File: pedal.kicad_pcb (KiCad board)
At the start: 4 copper layers, 39 parts, among them J2 USB_C_Receptacle_USB2.0_16P, SW1 MK-11C04-G013, U1 STM32H745XIH6, U2 TPS631000DRLR, U3 TLV77018PDBVR, U4 TPS2116DRL, U5 USBLC6-2SC6, U6 USBLC6-2SC6, U7 BQ25302, U8 BQ27427YZFR

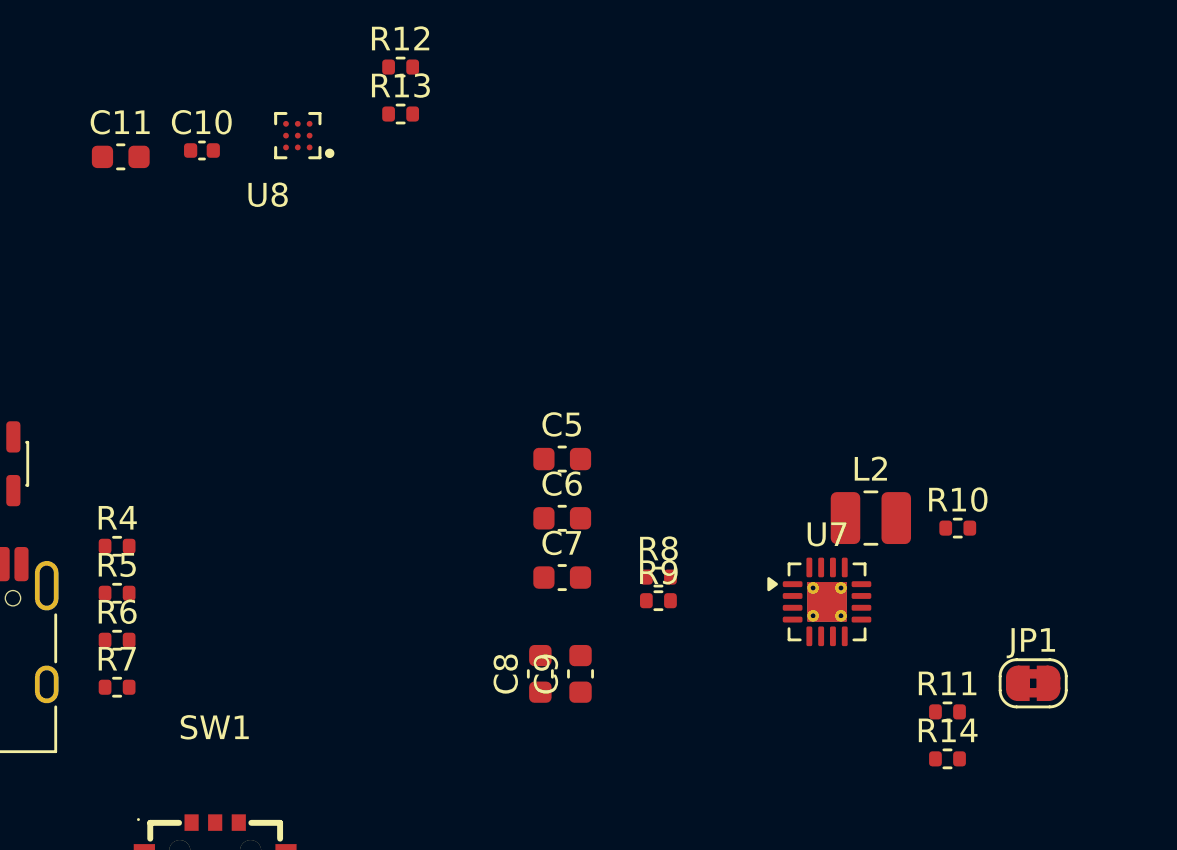
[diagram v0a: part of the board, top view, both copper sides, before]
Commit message: add battery connector model and charge led
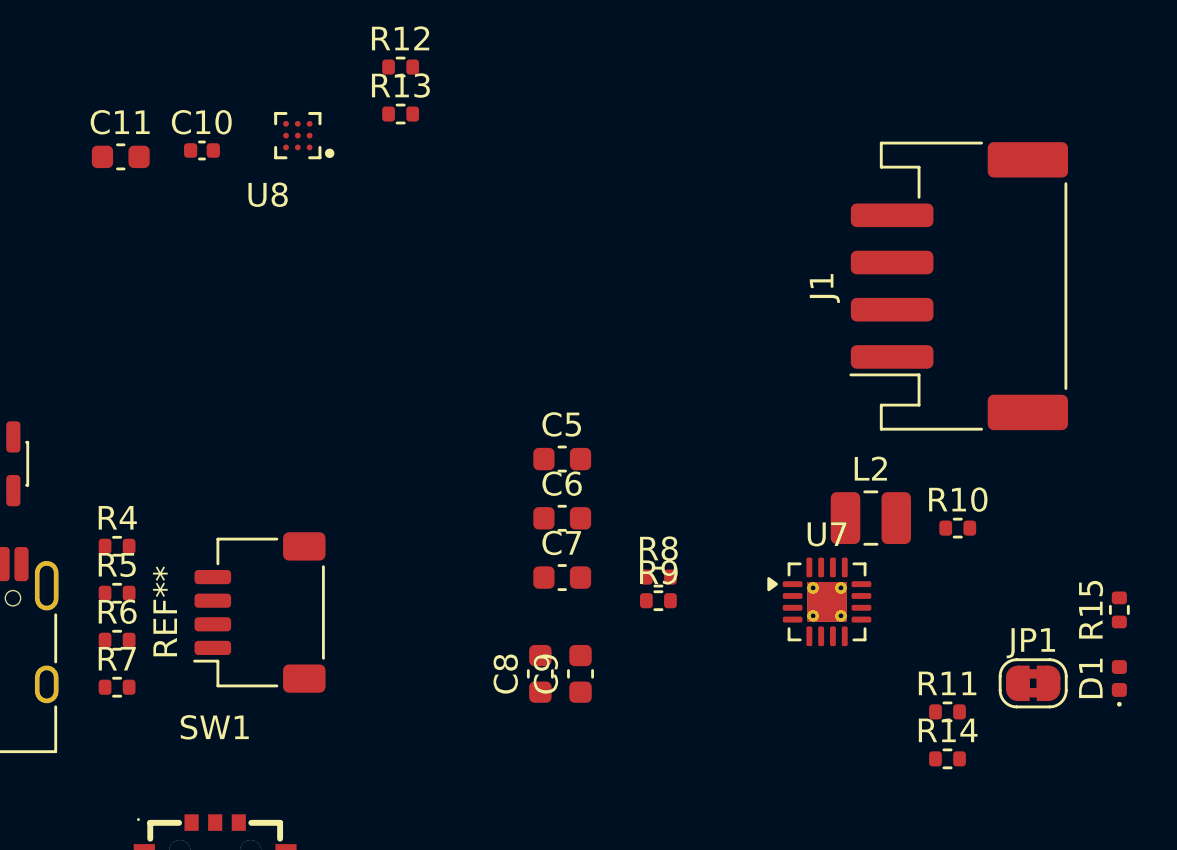
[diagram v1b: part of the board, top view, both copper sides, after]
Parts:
- added D1: CHARGE, LED_SMD:LED_0402_1005Metric, F.Cu at (192.4, 132.9)
- added J1: Battery, Connector_JST:JST_PH_S4B-PH-SM4-TB_1x04-1MP_P2.00mm_Horizontal, F.Cu at (185.6, 116.3)
- added R15: 2.4k, Resistor_SMD:R_0402_1005Metric, F.Cu at (192.4, 130.0)
- added REF**: JST_SH_SM04B-SRSS-TB_1x04-1MP_P1.00mm_Horizontal, Connector_JST:JST_SH_SM04B-SRSS-TB_1x04-1MP_P1.00mm_Horizontal, F.Cu at (156.0, 130.1)

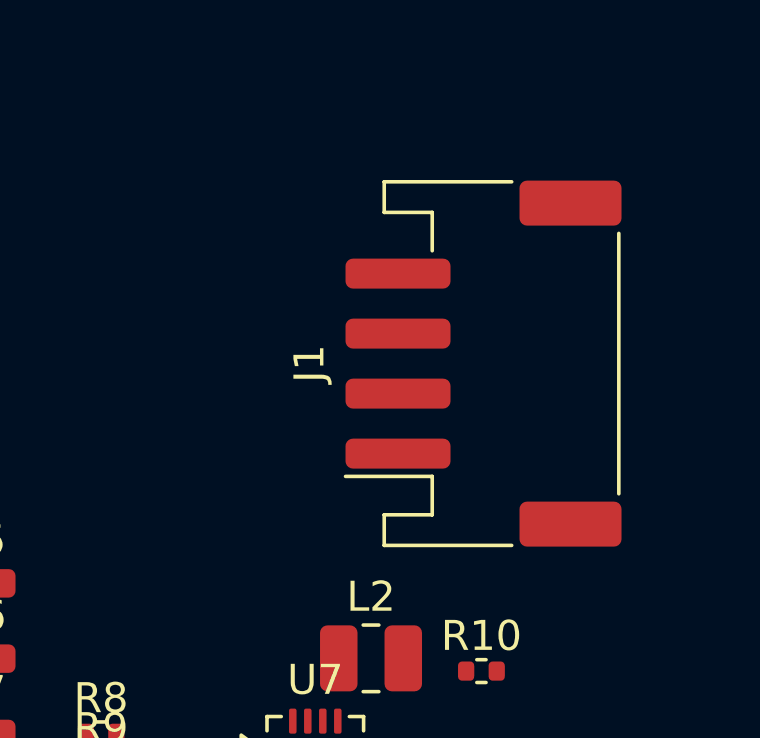
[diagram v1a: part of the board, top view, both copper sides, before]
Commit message: replace battery connector with solder pads
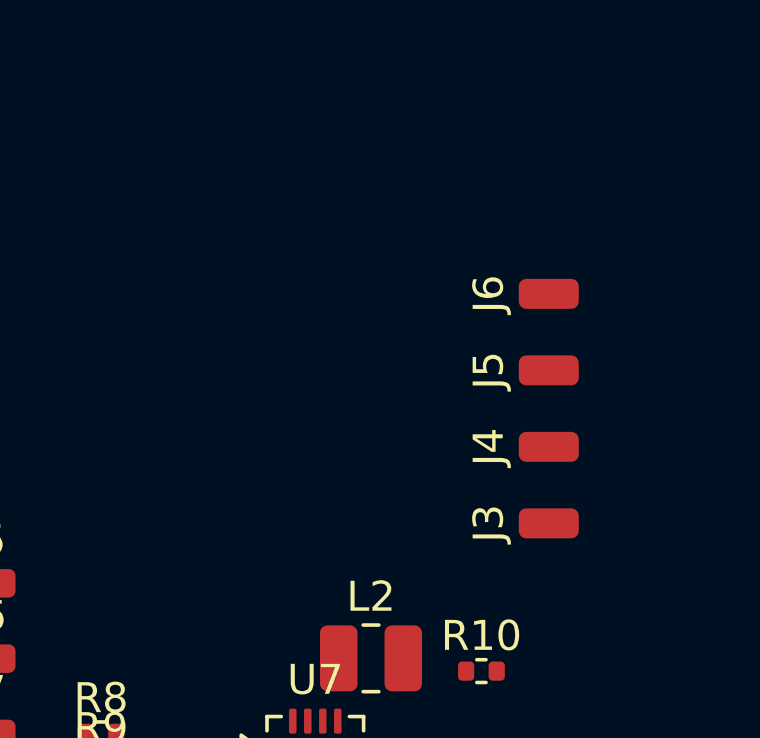
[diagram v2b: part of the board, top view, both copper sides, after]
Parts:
- removed J1: Battery, Connector_JST:JST_PH_S4B-PH-SM4-TB_1x04-1MP_P2.00mm_Horizontal
- added J3: VBATT, Connector_Wire:SolderWirePad_1x01_SMD_1x2mm, F.Cu at (187.8, 121.6)
- added J4: THERM, Connector_Wire:SolderWirePad_1x01_SMD_1x2mm, F.Cu at (187.8, 119.0)
- added J5: GND, Connector_Wire:SolderWirePad_1x01_SMD_1x2mm, F.Cu at (187.8, 116.5)
- added J6: GND, Connector_Wire:SolderWirePad_1x01_SMD_1x2mm, F.Cu at (187.8, 114.0)

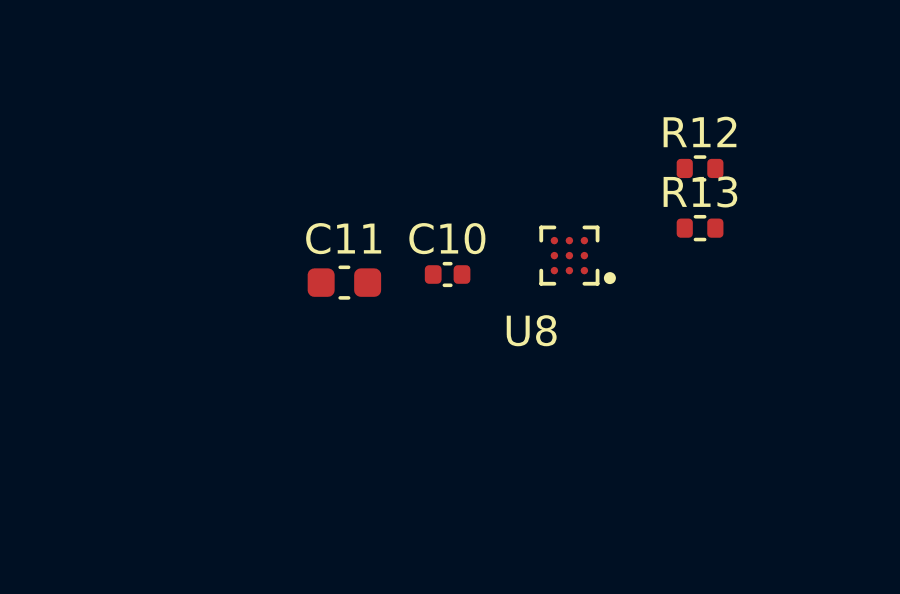
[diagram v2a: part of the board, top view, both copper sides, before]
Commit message: add microcontroller decoupling
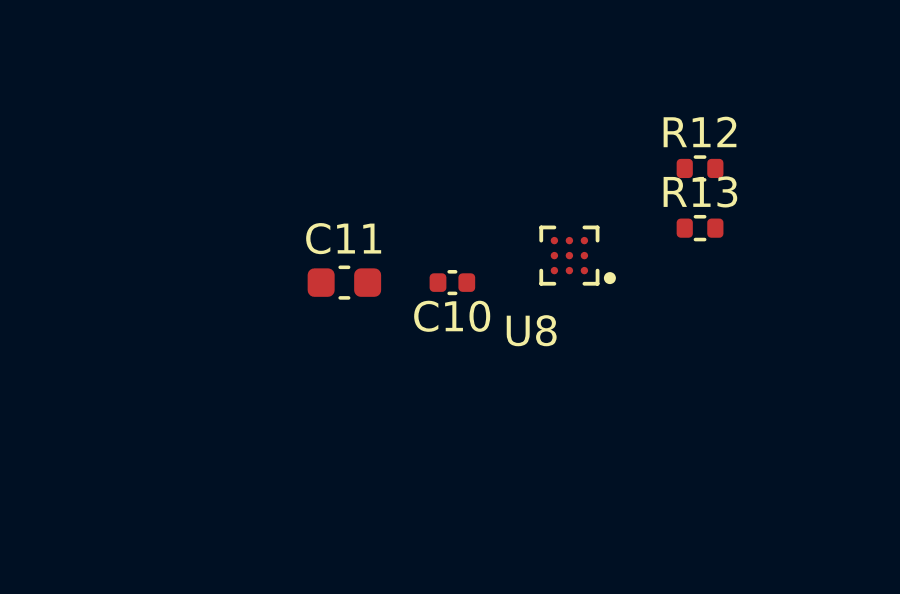
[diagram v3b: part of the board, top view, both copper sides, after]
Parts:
- moved C10 0.31 mm to (153.7, 110.8), turned to 180 degrees
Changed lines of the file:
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@@
 	(footprint "Capacitor_SMD:C_0402_1005Metric"
 		(layer "F.Cu")
-		(at 153.54 110.53)
+		(at 153.7 110.8 180)
 		(descr "Capacitor SMD 0402 (1005 Metric), square (rectangular) end terminal, IPC-7351 nominal, (Body size source: IPC-SM-782 page 76, https://www.pcb-3d.com/wordpress/wp-content/uploads/ipc-sm-782a_amendment_1_and_2.pdf)")
 		(tags "capacitor")
@@
 		)
 		(property "LCSC" "C52923"
-			(at 0 0 0)
+			(at 0 0 180)
 			(unlocked yes)
 			(layer "F.Fab")
@@
 		)
 		(property "voltage" "25"
-			(at 0 0 0)
+			(at 0 0 180)
 			(unlocked yes)
 			(layer "F.Fab")
@@
 		(duplicate_pad_numbers_are_jumpers no)
 		(fp_line
-			(start -0.107836 -0.36)
-			(end 0.107836 -0.36)
+			(start -0.107836 0.36)
+			(end 0.107836 0.36)
 			(stroke
 				(width 0.12)
@@
 		)
 		(fp_line
-			(start -0.107836 0.36)
-			(end 0.107836 0.36)
+			(start -0.107836 -0.36)
+			(end 0.107836 -0.36)
 			(stroke
 				(width 0.12)
@@
 		)
 		(pad "1" smd roundrect
-			(at -0.48 0)
+			(at -0.48 0 180)
 			(size 0.56 0.62)
 			(layers "F.Cu" "F.Mask" "F.Paste")
@@
 		)
 		(pad "2" smd roundrect
-			(at 0.48 0)
+			(at 0.48 0 180)
 			(size 0.56 0.62)
 			(layers "F.Cu" "F.Mask" "F.Paste")

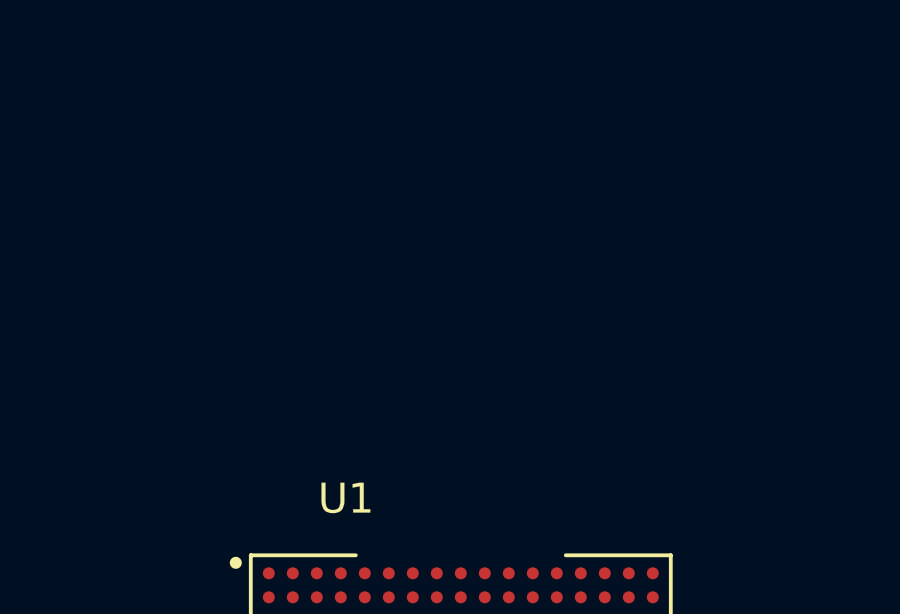
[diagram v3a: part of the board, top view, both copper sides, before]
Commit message: add decoupling caps
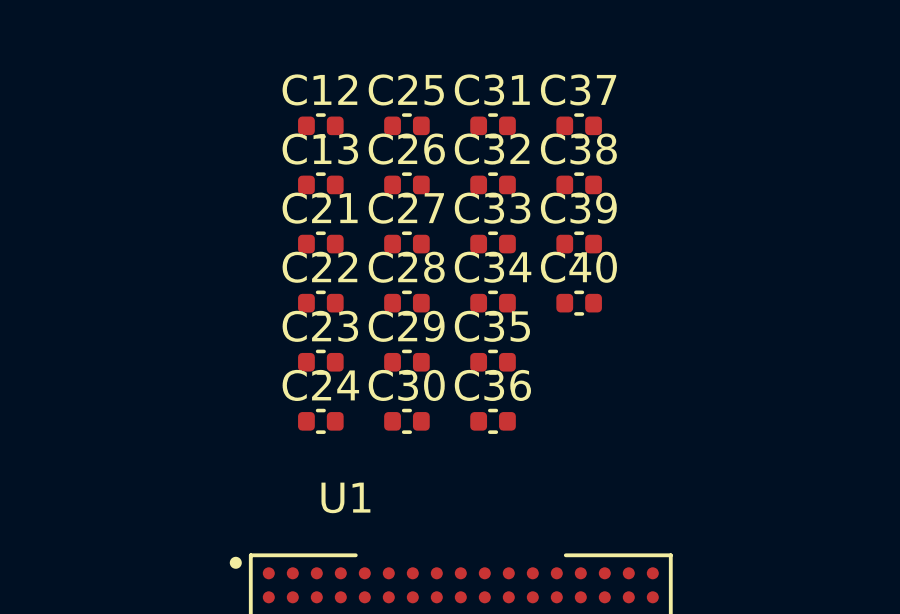
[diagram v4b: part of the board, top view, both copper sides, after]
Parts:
- added C12: 4.7uF, Capacitor_SMD:C_0402_1005Metric, F.Cu at (120.0, 92.0)
- added C13: 4.7uF, Capacitor_SMD:C_0402_1005Metric, F.Cu at (120.0, 94.0)
- added C21: 1uF, Capacitor_SMD:C_0402_1005Metric, F.Cu at (120.0, 95.9)
- added C22: 1uF, Capacitor_SMD:C_0402_1005Metric, F.Cu at (120.0, 97.9)
- added C23: 1uF, Capacitor_SMD:C_0402_1005Metric, F.Cu at (120.0, 99.9)
- added C24: 1uF, Capacitor_SMD:C_0402_1005Metric, F.Cu at (120.0, 101.8)
- added C25: 1uF, Capacitor_SMD:C_0402_1005Metric, F.Cu at (122.9, 92.0)
- added C26: 1uF, Capacitor_SMD:C_0402_1005Metric, F.Cu at (122.9, 94.0)
- added C27: 1uF, Capacitor_SMD:C_0402_1005Metric, F.Cu at (122.9, 95.9)
- added C28: 1uF, Capacitor_SMD:C_0402_1005Metric, F.Cu at (122.9, 97.9)
- added C29: 1uF, Capacitor_SMD:C_0402_1005Metric, F.Cu at (122.9, 99.9)
- added C30: 1uF, Capacitor_SMD:C_0402_1005Metric, F.Cu at (122.9, 101.8)
- added C31: 1uF, Capacitor_SMD:C_0402_1005Metric, F.Cu at (125.8, 92.0)
- added C32: 1uF, Capacitor_SMD:C_0402_1005Metric, F.Cu at (125.8, 94.0)
- added C33: 1uF, Capacitor_SMD:C_0402_1005Metric, F.Cu at (125.8, 95.9)
- added C34: 1uF, Capacitor_SMD:C_0402_1005Metric, F.Cu at (125.8, 97.9)
- added C35: 1uF, Capacitor_SMD:C_0402_1005Metric, F.Cu at (125.8, 99.9)
- added C36: 1uF, Capacitor_SMD:C_0402_1005Metric, F.Cu at (125.8, 101.8)
- added C37: 1uF, Capacitor_SMD:C_0402_1005Metric, F.Cu at (128.6, 92.0)
- added C38: 1uF, Capacitor_SMD:C_0402_1005Metric, F.Cu at (128.6, 94.0)
- added C39: 1uF, Capacitor_SMD:C_0402_1005Metric, F.Cu at (128.6, 95.9)
- added C40: 1uF, Capacitor_SMD:C_0402_1005Metric, F.Cu at (128.6, 97.9)
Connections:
- U1 pad A1: VSS_1 -> GND
- U1 pad A17: VSS_1 -> GND
- U1 pad A6: VDDLDO -> +3V3
- U1 pad B1: unconnected-(U1C-VBAT-PadB1) -> +3V3
- U1 pad B2: VSS_1 -> GND
- U1 pad B6: VSS_1 -> GND
- U1 pad C10: VSS_1 -> GND
- U1 pad C13: VSS_1 -> GND
- U1 pad C16: VSS_1 -> GND
- U1 pad C17: VDDLDO -> +3V3
- U1 pad E11: VDD_1 -> +3V3
- U1 pad E6: VDD_1 -> +3V3
- U1 pad E9: VDD_1 -> +3V3
- U1 pad F17: unconnected-(U1C-VDD33USB-PadF17) -> +3V3
- U1 pad F5: VDD_1 -> +3V3
- U1 pad G10: VSS_2 -> GND
- U1 pad G11: VSS_2 -> GND
- U1 pad G13: VDD_1 -> +3V3
- U1 pad G16: VSS_1 -> GND
- U1 pad G5: VDD_1 -> +3V3
- U1 pad G7: VSS_1 -> GND
- U1 pad G8: VSS_1 -> GND
- U1 pad G9: VSS_1 -> GND
- U1 pad H10: VSS_2 -> GND
- U1 pad H11: VSS_2 -> GND
- U1 pad H13: VDD_1 -> +3V3
- U1 pad H5: VDD_1 -> +3V3
- U1 pad H7: VSS_2 -> GND
- U1 pad H8: VSS_2 -> GND
- U1 pad H9: VSS_2 -> GND
- U1 pad J10: VSS_2 -> GND
- U1 pad J11: VSS_2 -> GND
- U1 pad J13: VDD_1 -> +3V3
- U1 pad J16: VSS_1 -> GND
- U1 pad J17: VSS_1 -> GND
- U1 pad J3: VSS_1 -> GND
- U1 pad J7: VSS_2 -> GND
- U1 pad J8: VSS_2 -> GND
- U1 pad J9: VSS_2 -> GND
- U1 pad K10: VSS_2 -> GND
- U1 pad K11: VSS_2 -> GND
- U1 pad K13: VDD_1 -> +3V3
- U1 pad K15: VSS_1 -> GND
- U1 pad K5: VDD_1 -> +3V3
- U1 pad K7: VSS_2 -> GND
- U1 pad K8: VSS_2 -> GND
- U1 pad K9: VSS_2 -> GND
- U1 pad L1: unconnected-(U1C-VDDA-PadL1) -> +3V3
- U1 pad L10: VSS_2 -> GND
- U1 pad L11: VSS_2 -> GND
- U1 pad L13: VDD_2 -> +3V3
- U1 pad L15: VSS_1 -> GND
- U1 pad L5: VDD_2 -> +3V3
- U1 pad L7: VSS_2 -> GND
- U1 pad L8: VSS_2 -> GND
- U1 pad L9: VSS_2 -> GND
- U1 pad M1: unconnected-(U1C-VREF+-PadM1) -> +3V3
- U1 pad M13: VDD_2 -> +3V3
- U1 pad M15: VSS_1 -> GND
- U1 pad M5: VDD_2 -> +3V3
- U1 pad N1: unconnected-(U1C-VREF--PadN1) -> GND
- U1 pad N10: VDD_2 -> +3V3
- U1 pad N11: VDD_2 -> +3V3
- U1 pad N12: VDD_2 -> +3V3
- U1 pad N16: VSS_1 -> GND
- U1 pad N7: VDD_2 -> +3V3
- U1 pad N8: VDD_2 -> +3V3
- U1 pad P1: unconnected-(U1C-VSSA-PadP1) -> GND
- U1 pad P17: VDD_2 -> +3V3
- U1 pad R4: VSS_1 -> GND
- U1 pad R8: VSS_1 -> GND
- U1 pad T12: VSS_1 -> GND
- U1 pad U1: VSS_1 -> GND
- U1 pad U12: VDDLDO -> +3V3
- U1 pad U17: VSS_1 -> GND
